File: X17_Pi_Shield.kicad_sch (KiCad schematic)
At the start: 7 parts, among them J1 BM04B-GHS-TBT, U1 RASPBERRY_PI_4B_4GB, U2 BNO080, U3 AZ1117IH-3.3TRG1

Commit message: Hierarchy Schematic Update
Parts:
- removed Bar02: DF13-4P-1.25DSA, CON4_1X4_U_DF13, symbol DF13_4P_1_25DSA:DF13-4P-1.25DSA
- removed C1: 10uF, symbol Device:C_Polarized
- removed C2: 22uF, symbol Device:C_Polarized
- removed J1: BM04B-GHS-TBT, CONN_BM04B-GHS-TBT_JST, symbol BM04B_GHS_TBT:BM04B-GHS-TBT
- removed U1: RASPBERRY_PI_4B_4GB, RASPBERRY_PI_4B_4GB:MODULE_RASPBERRY_PI_4B_4GB, symbol RASPBERRY_PI_4B_4GB:RASPBERRY_PI_4B_4GB
- removed U2: BNO080, BNO080:IC_BNO080, symbol BNO080:BNO080
- removed U3: AZ1117IH-3.3TRG1, AZ1117IH-3.3TRG1:SOT230P700X185-4N, symbol AZ1117IH-3.3TRG1:AZ1117IH-3.3TRG1
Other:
- added sheet Pi + IMU (pi_imu.kicad_sch)
- added sheet Power (power.kicad_sch)
- added sheet Sensors (Sensors.kicad_sch)

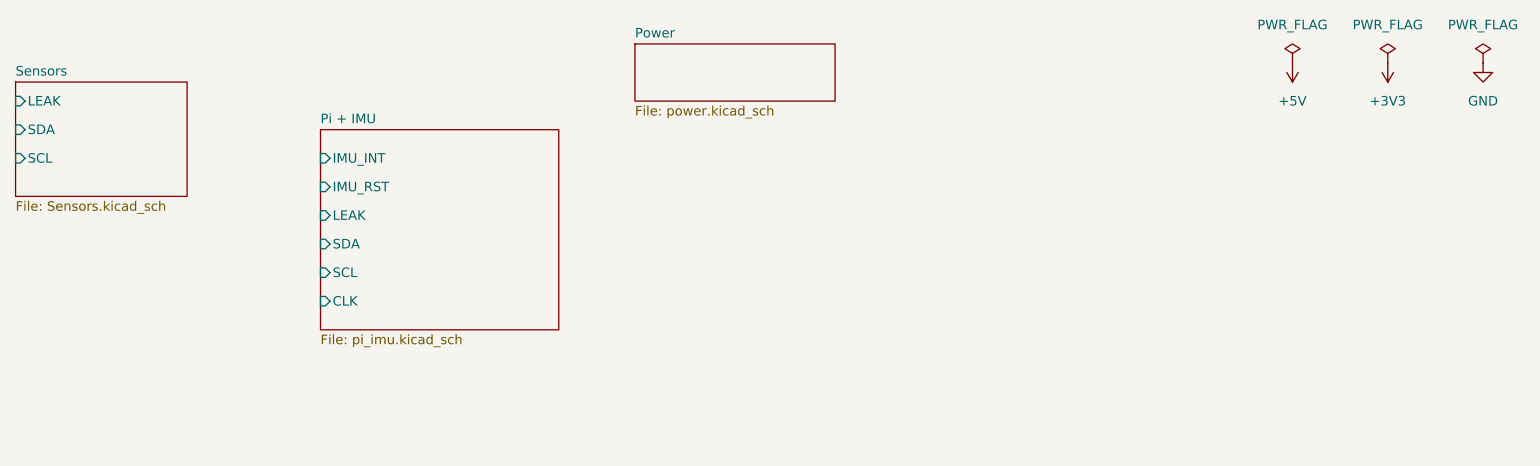
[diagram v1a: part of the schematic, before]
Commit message: Added New Libraries and Schematic Updates
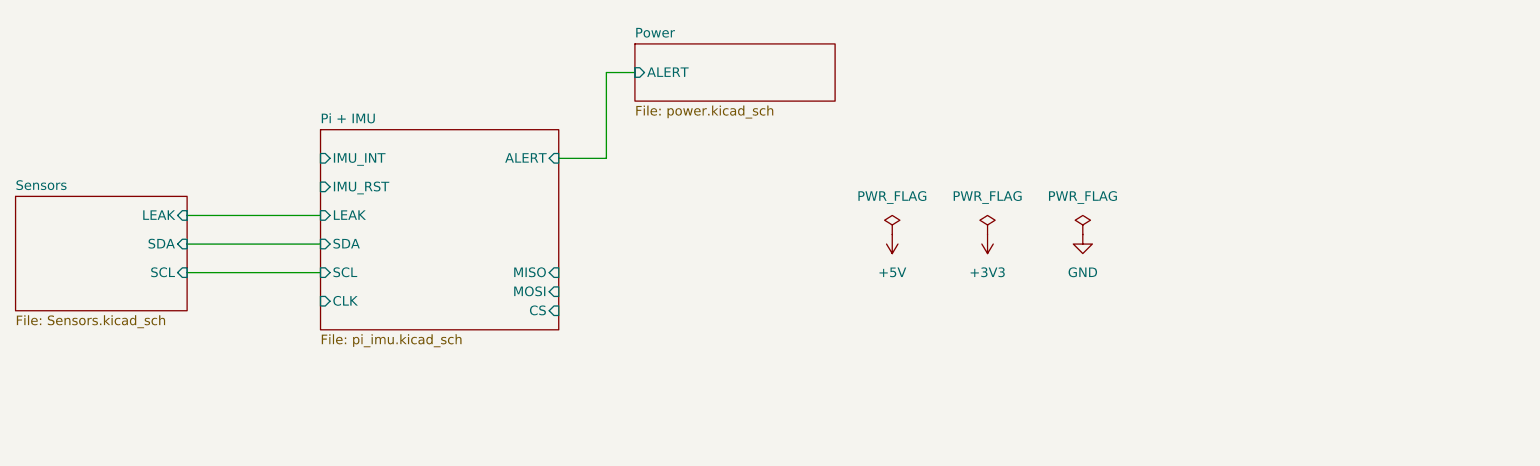
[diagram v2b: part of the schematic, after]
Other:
- sheet Pi + IMU ports: added ALERT, CS, MISO, MOSI; removed none
- sheet Power ports: added ALERT; removed none
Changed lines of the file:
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@@
+		)
+	)
+	(wire
+		(pts
+			(xy 74.93 49.53) (xy 92.71 49.53)
+		)
+		(stroke
+			(width 0)
+			(type default)
+		)
+	)
+	(wire
+		(pts
+			(xy 74.93 41.91) (xy 92.71 41.91)
+		)
+		(stroke
+			(width 0)
+			(type default)
+		)
+	)
+	(wire
+		(pts
+			(xy 130.81 22.86) (xy 130.81 34.29)
+		)
+		(stroke
+			(width 0)
+			(type default)
+		)
+	)
+	(wire
+		(pts
+			(xy 134.62 22.86) (xy 130.81 22.86)
+		)
+		(stroke
+			(width 0)
+			(type default)
+		)
+	)
+	(wire
+		(pts
+			(xy 130.81 34.29) (xy 124.46 34.29)
+		)
+		(stroke
+			(width 0)
+			(type default)
+		)
+	)
+	(wire
+		(pts
+			(xy 74.93 45.72) (xy 92.71 45.72)
+		)
+		(stroke
+			(width 0)
+			(type default)
 		)
 	)
 	(symbol
 		(lib_id "power:PWR_FLAG")
-		(at 234.95 21.59 0)
+		(at 181.61 44.45 0)
 		(unit 1)
 		(exclude_from_sim no)
@@
 		(fields_autoplaced yes)
 		(property "Reference" "#FLG02"
-			(at 234.95 19.685 0)
+			(at 181.61 42.545 0)
 			(effects
 				(font
@@
 		)
 		(property "Value" "PWR_FLAG"
-			(at 234.95 16.51 0)
+			(at 181.61 39.37 0)
 			(effects
 				(font
@@
 		)
 		(property "Footprint" ""
-			(at 234.95 21.59 0)
+			(at 181.61 44.45 0)
 			(effects
 				(font
@@
 		)
 		(property "Datasheet" "~"
-			(at 234.95 21.59 0)
+			(at 181.61 44.45 0)
 			(effects
 				(font
@@
 		)
 		(property "Description" "Special symbol for telling ERC where power comes from"
-			(at 234.95 21.59 0)
+			(at 181.61 44.45 0)
 			(effects
 				(font
@@
 	(symbol
 		(lib_id "power:+5V")
-		(at 222.25 21.59 180)
+		(at 168.91 44.45 180)
 		(unit 1)
 		(exclude_from_sim no)
@@
 		(fields_autoplaced yes)
 		(property "Reference" "#PWR04"
-			(at 222.25 17.78 0)
+			(at 168.91 40.64 0)
 			(effects
 				(font
@@
 		)
 		(property "Value" "+5V"
-			(at 222.25 26.67 0)
+			(at 168.91 49.53 0)
 			(effects
 				(font
@@
 		)
 		(property "Footprint" ""
-			(at 222.25 21.59 0)
+			(at 168.91 44.45 0)
 			(effects
 				(font
@@
 		)
 		(property "Datasheet" ""
-			(at 222.25 21.59 0)
+			(at 168.91 44.45 0)
 			(effects
 				(font
@@
 		)
 		(property "Description" "Power symbol creates a global label with name \"+5V\""
-			(at 222.25 21.59 0)
+			(at 168.91 44.45 0)
 			(effects
 				(font
@@
 	(symbol
 		(lib_id "power:PWR_FLAG")
-		(at 247.65 21.59 0)
+		(at 194.31 44.45 0)
 		(unit 1)
 		(exclude_from_sim no)
@@
 		(fields_autoplaced yes)
 		(property "Reference" "#FLG03"
-			(at 247.65 19.685 0)
+			(at 194.31 42.545 0)
 			(effects
 				(font
@@
 		)
 		(property "Value" "PWR_FLAG"
-			(at 247.65 16.51 0)
+			(at 194.31 39.37 0)
 			(effects
 				(font
@@
 		)
 		(property "Footprint" ""
-			(at 247.65 21.59 0)
+			(at 194.31 44.45 0)
 			(effects
 				(font
@@
 		)
 		(property "Datasheet" "~"
-			(at 247.65 21.59 0)
+			(at 194.31 44.45 0)
 			(effects
 				(font
@@
 		)
 		(property "Description" "Special symbol for telling ERC where power comes from"
-			(at 247.65 21.59 0)
+			(at 194.31 44.45 0)
 			(effects
 				(font
@@
 	(symbol
 		(lib_id "power:PWR_FLAG")
-		(at 222.25 21.59 0)
+		(at 168.91 44.45 0)
 		(unit 1)
 		(exclude_from_sim no)
@@
 		(fields_autoplaced yes)
 		(property "Reference" "#FLG01"
-			(at 222.25 19.685 0)
+			(at 168.91 42.545 0)
 			(effects
 				(font
@@
 		)
 		(property "Value" "PWR_FLAG"
-			(at 222.25 16.51 0)
+			(at 168.91 39.37 0)
 			(effects
 				(font
@@
 		)
 		(property "Footprint" ""
-			(at 222.25 21.59 0)
+			(at 168.91 44.45 0)
 			(effects
 				(font
@@
 		)
 		(property "Datasheet" "~"
-			(at 222.25 21.59 0)
+			(at 168.91 44.45 0)
 			(effects
 				(font
@@
 		)
 		(property "Description" "Special symbol for telling ERC where power comes from"
-			(at 222.25 21.59 0)
+			(at 168.91 44.45 0)
 			(effects
 				(font
@@
 	(symbol
 		(lib_id "power:GND")
-		(at 247.65 21.59 0)
+		(at 194.31 44.45 0)
 		(unit 1)
 		(exclude_from_sim no)
@@
 		(fields_autoplaced yes)
 		(property "Reference" "#PWR06"
-			(at 247.65 27.94 0)
+			(at 194.31 50.8 0)
 			(effects
 				(font
@@
 		)
 		(property "Value" "GND"
-			(at 247.65 26.67 0)
+			(at 194.31 49.53 0)
 			(effects
 				(font
@@
 		)
 		(property "Footprint" ""
-			(at 247.65 21.59 0)
+			(at 194.31 44.45 0)
 			(effects
 				(font
@@
 		)
 		(property "Datasheet" ""
-			(at 247.65 21.59 0)
+			(at 194.31 44.45 0)
 			(effects
 				(font
@@
 		)
 		(property "Description" "Power symbol creates a global label with name \"GND\" , ground"
-			(at 247.65 21.59 0)
+			(at 194.31 44.45 0)
 			(effects
 				(font
@@
 	(symbol
 		(lib_id "power:+3V3")
-		(at 234.95 21.59 180)
+		(at 181.61 44.45 180)
 		(unit 1)
 		(exclude_from_sim no)
@@
 		(fields_autoplaced yes)
 		(property "Reference" "#PWR05"
-			(at 234.95 17.78 0)
+			(at 181.61 40.64 0)
 			(effects
 				(font
@@
 		)
 		(property "Value" "+3V3"
-			(at 234.95 26.67 0)
+			(at 181.61 49.53 0)
 			(effects
 				(font
@@
 		)
 		(property "Footprint" ""
-			(at 234.95 21.59 0)
+			(at 181.61 44.45 0)
 			(effects
 				(font
@@
 		)
 		(property "Datasheet" ""
-			(at 234.95 21.59 0)
+			(at 181.61 44.45 0)
 			(effects
 				(font
@@
 		)
 		(property "Description" "Power symbol creates a global label with name \"+3V3\""
-			(at 234.95 21.59 0)
+			(at 181.61 44.45 0)
 			(effects
 				(font
@@
 			)
 		)
+		(pin "ALERT" input
+			(at 124.46 34.29 0)
+			(effects
+				(font
+					(size 1.27 1.27)
+				)
+				(justify right)
+			)
+		)
+		(pin "MISO" input
+			(at 124.46 49.53 0)
+			(effects
+				(font
+					(size 1.27 1.27)
+				)
+				(justify right)
+			)
+		)
+		(pin "MOSI" input
+			(at 124.46 52.07 0)
+			(effects
+				(font
+					(size 1.27 1.27)
+				)
+				(justify right)
+			)
+		)
+		(pin "CS" input
+			(at 124.46 54.61 0)
+			(effects
+				(font
+					(size 1.27 1.27)
+				)
+				(justify right)
+			)
+		)
 		(instances
 			(project "X17_Pi_Shield"
@@
 	)
 	(sheet
-		(at 52.07 24.13)
+		(at 52.07 39.37)
 		(size 22.86 15.24)
 		(fields_autoplaced yes)
@@
 		)
 		(property "Sheetname" "Sensors"
-			(at 52.07 23.4184 0)
+			(at 52.07 38.6584 0)
 			(effects
 				(font
@@
 		)
 		(property "Sheetfile" "Sensors.kicad_sch"
-			(at 52.07 39.9546 0)
+			(at 52.07 55.1946 0)
 			(effects
 				(font
@@
 		)
 		(pin "LEAK" input
-			(at 52.07 26.67 180)
-			(effects
-				(font
-					(size 1.27 1.27)
-				)
-				(justify left)
+			(at 74.93 41.91 0)
+			(effects
+				(font
+					(size 1.27 1.27)
+				)
+				(justify right)
 			)
 		)
 		(pin "SDA" input
-			(at 52.07 30.48 180)
-			(effects
-				(font
-					(size 1.27 1.27)
-				)
-				(justify left)
+			(at 74.93 45.72 0)
+			(effects
+				(font
+					(size 1.27 1.27)
+				)
+				(justify right)
 			)
 		)
 		(pin "SCL" input
-			(at 52.07 34.29 180)
-			(effects
-				(font
-					(size 1.27 1.27)
-				)
-				(justify left)
+			(at 74.93 49.53 0)
+			(effects
+				(font
+					(size 1.27 1.27)
+				)
+				(justify right)
 			)
 		)
@@
 			)
 		)
+		(pin "ALERT" input
+			(at 134.62 22.86 180)
+			(effects
+				(font
+					(size 1.27 1.27)
+				)
+				(justify left)
+			)
+		)

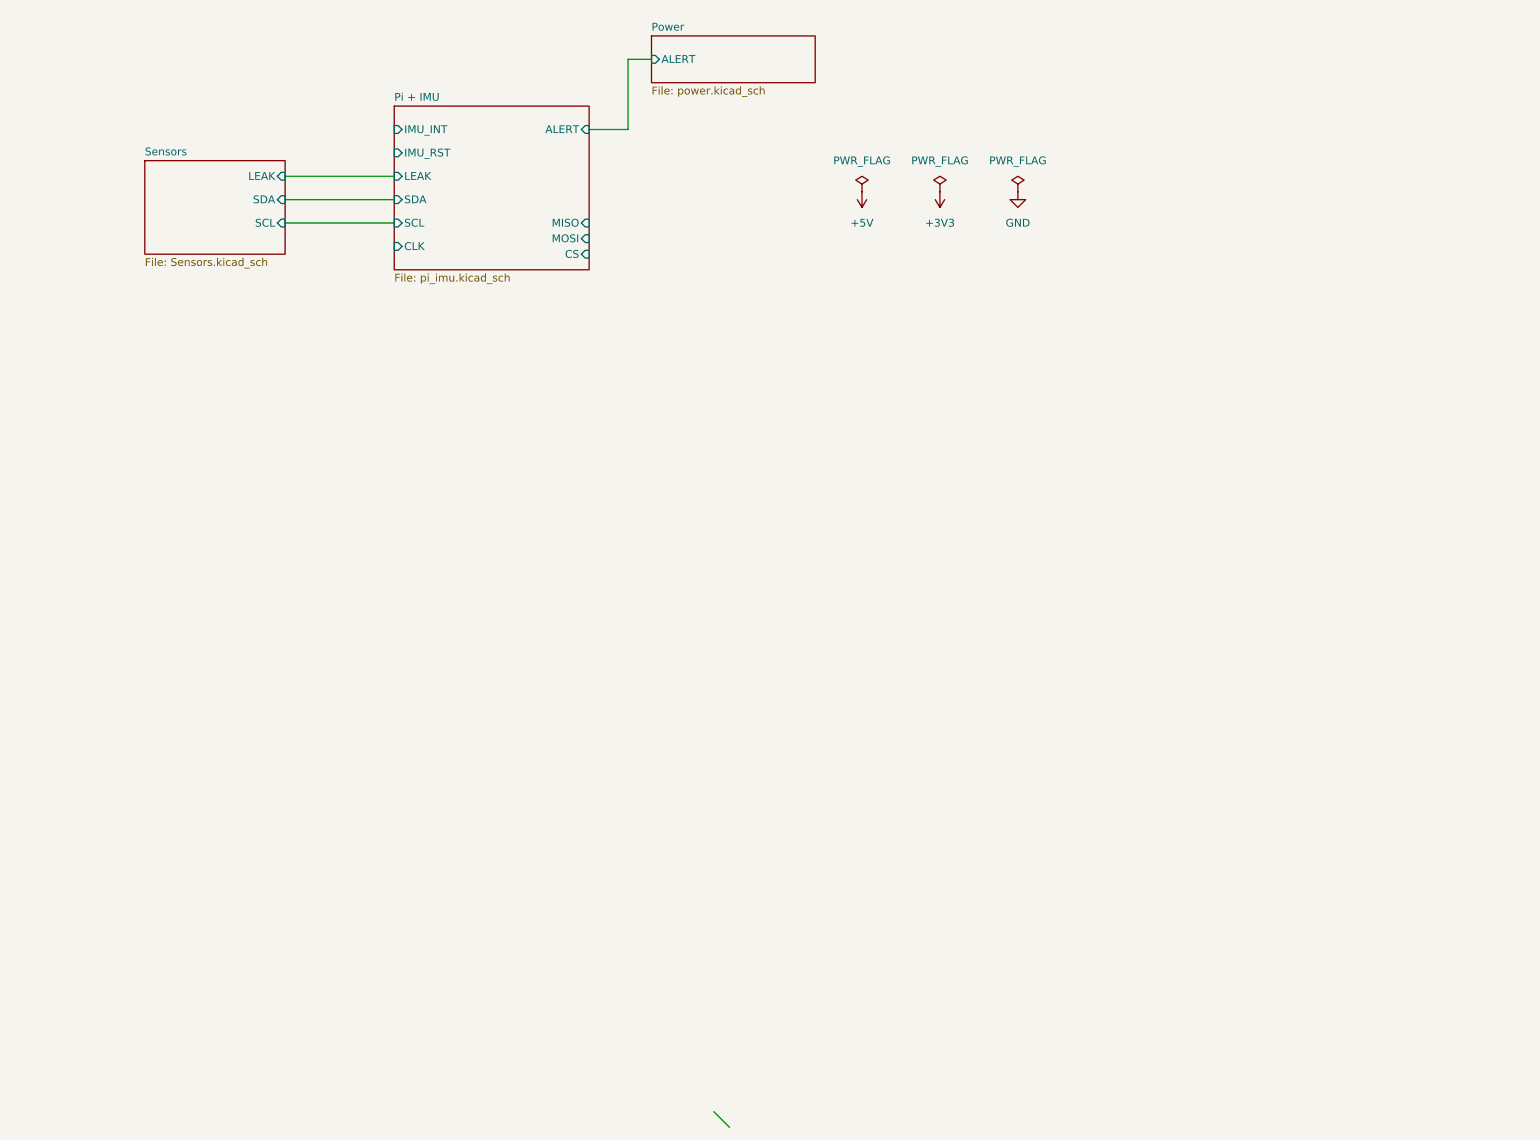
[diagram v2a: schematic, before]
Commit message: Root Update and Adding ISO Pt1
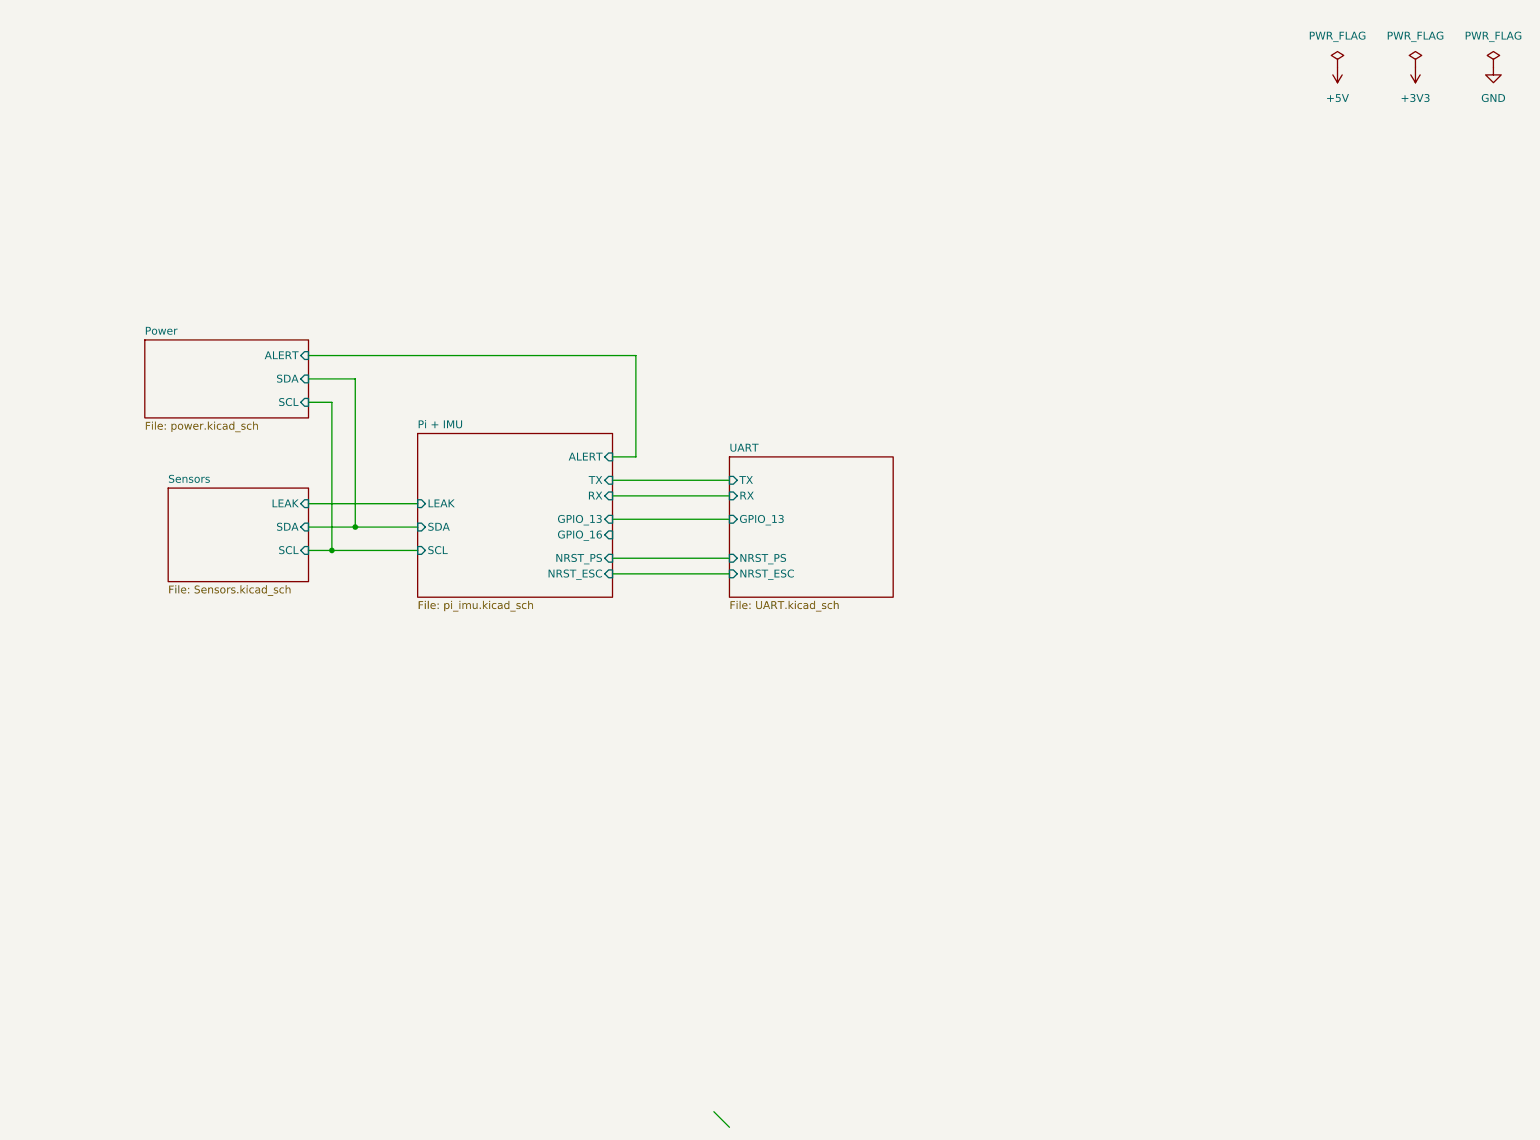
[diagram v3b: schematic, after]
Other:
- added sheet UART (UART.kicad_sch)
- sheet Pi + IMU ports: added GPIO_13, GPIO_16, NRST_ESC, NRST_PS, RX, TX; removed CLK, CS, IMU_INT, IMU_RST, MISO, MOSI
- sheet Power ports: added SCL, SDA; removed none

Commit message: Adding Libraries
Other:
- sheet Pi + IMU ports: added BKP_EN, TB_EN; removed GPIO_13, GPIO_16
- sheet Power ports: added 5V_BACKPLANE; removed none
- sheet UART ports: added 5V_BACKPLANE, BKP_EN, TB_EN; removed GPIO_13
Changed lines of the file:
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@@
+	(wire
+		(pts
+			(xy 179.07 91.44) (xy 179.07 63.5)
+		)
+		(stroke
+			(width 0)
+			(type default)
+		)
+	)
+	(wire
+		(pts
+			(xy 128.27 97.79) (xy 147.32 97.79)
+		)
+		(stroke
+			(width 0)
+			(type default)
+		)
+	)
 	(wire
 		(pts
@@
 	(wire
 		(pts
+			(xy 48.26 71.12) (xy 52.07 71.12)
+		)
+		(stroke
+			(width 0)
+			(type default)
+		)
+	)
+	(wire
+		(pts
 			(xy 86.36 99.06) (xy 96.52 99.06)
 		)
@@
 	(wire
 		(pts
+			(xy 48.26 63.5) (xy 48.26 71.12)
+		)
+		(stroke
+			(width 0)
+			(type default)
+		)
+	)
+	(wire
+		(pts
 			(xy 128.27 93.98) (xy 147.32 93.98)
 		)
@@
 	(wire
 		(pts
-			(xy 128.27 97.79) (xy 147.32 97.79)
+			(xy 179.07 63.5) (xy 48.26 63.5)
 		)
 		(stroke
@@
 	(wire
 		(pts
+			(xy 173.99 91.44) (xy 179.07 91.44)
+		)
+		(stroke
+			(width 0)
+			(type default)
+		)
+	)
+	(wire
+		(pts
 			(xy 78.74 78.74) (xy 82.55 78.74)
 		)
@@
 		(pts
 			(xy 78.74 74.93) (xy 86.36 74.93)
+		)
+		(stroke
+			(width 0)
+			(type default)
+		)
+	)
+	(wire
+		(pts
+			(xy 128.27 100.33) (xy 147.32 100.33)
 		)
 		(stroke
@@
 			)
 		)
-		(pin "GPIO_13" input
-			(at 128.27 97.79 0)
-			(effects
-				(font
-					(size 1.27 1.27)
-				)
-				(justify right)
-			)
-		)
 		(pin "TX" input
 			(at 128.27 91.44 0)
@@
 			)
 		)
-		(pin "GPIO_16" input
-			(at 128.27 100.33 0)
-			(effects
-				(font
-					(size 1.27 1.27)
-				)
-				(justify right)
-			)
-		)
 		(pin "NRST_ESC" input
 			(at 128.27 106.68 0)
+			(effects
+				(font
+					(size 1.27 1.27)
+				)
+				(justify right)
+			)
+		)
+		(pin "BKP_EN" input
+			(at 128.27 97.79 0)
+			(effects
+				(font
+					(size 1.27 1.27)
+				)
+				(justify right)
+			)
+		)
+		(pin "TB_EN" input
+			(at 128.27 100.33 0)
 			(effects
 				(font
@@
 			)
 		)
-		(pin "GPIO_13" input
-			(at 147.32 97.79 180)
-			(effects
-				(font
-					(size 1.27 1.27)
-				)
-				(justify left)
-			)
-		)
 		(pin "TX" input
 			(at 147.32 91.44 180)
@@
 				)
 				(justify left)
+			)
+		)
+		(pin "BKP_EN" input
+			(at 147.32 97.79 180)
+			(effects
+				(font
+					(size 1.27 1.27)
+				)
+				(justify left)
+			)
+		)
+		(pin "TB_EN" input
+			(at 147.32 100.33 180)
+			(effects
+				(font
+					(size 1.27 1.27)
+				)
+				(justify left)
+			)
+		)
+		(pin "5V_BACKPLANE" input
+			(at 173.99 91.44 0)
+			(effects
+				(font
+					(size 1.27 1.27)
+				)
+				(justify right)
 			)
 		)
@@
 			)
 		)
+		(pin "5V_BACKPLANE" input
+			(at 52.07 71.12 180)
+			(effects
+				(font
+					(size 1.27 1.27)
+				)
+				(justify left)
+			)
+		)
